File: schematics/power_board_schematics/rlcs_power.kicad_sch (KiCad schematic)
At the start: 44 parts, among them J1 Conn_01x05_Male, J2 Conn_01x05_Male, J3 Screw_Terminal_01x02, J4 Screw_Terminal_01x02, J5 Battery Conn, J6 Screw_Terminal_01x02, J7 Screw_Terminal_01x02, J8 CONN_01X02, Q1 Q_NPN_BEC, Q2 Q_NPN_BEC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

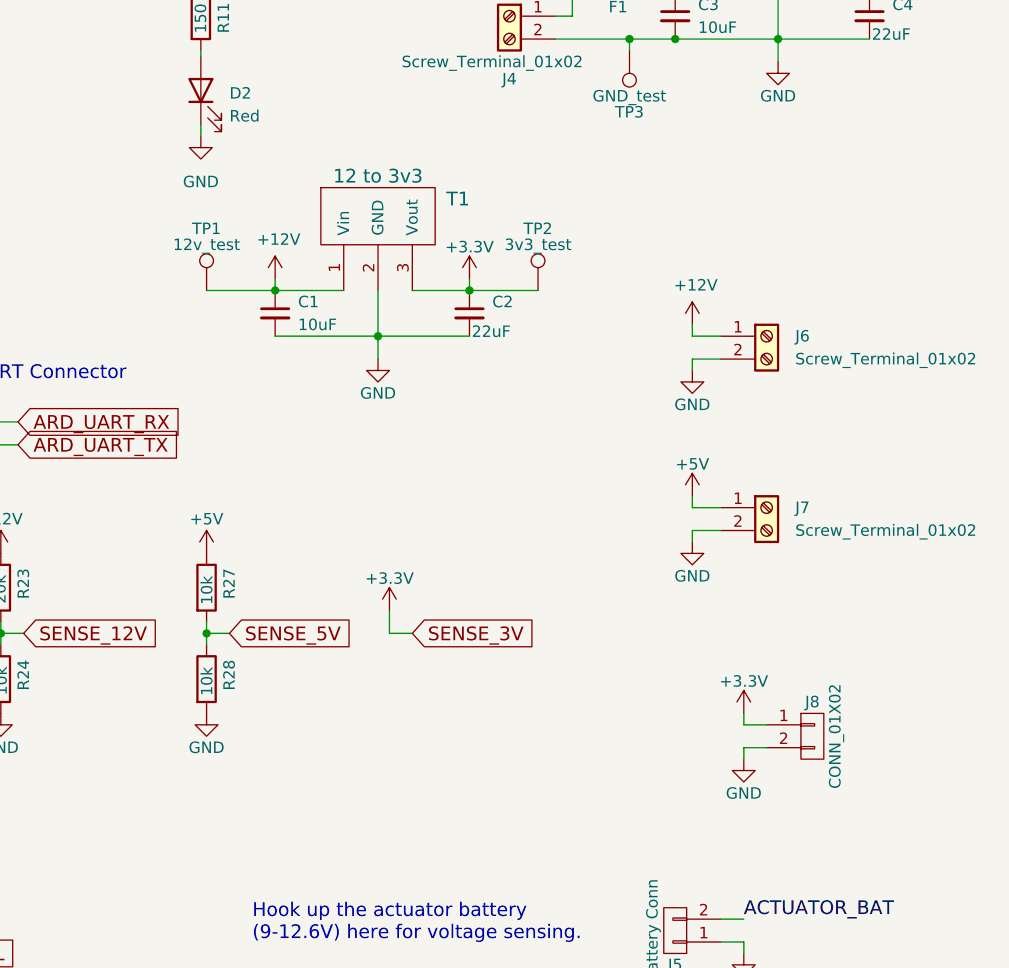
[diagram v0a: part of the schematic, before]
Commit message: Remove 3.3V circuit from Towerside Power Board
Remove 3.3V regulator
Remove 3.3V sensing
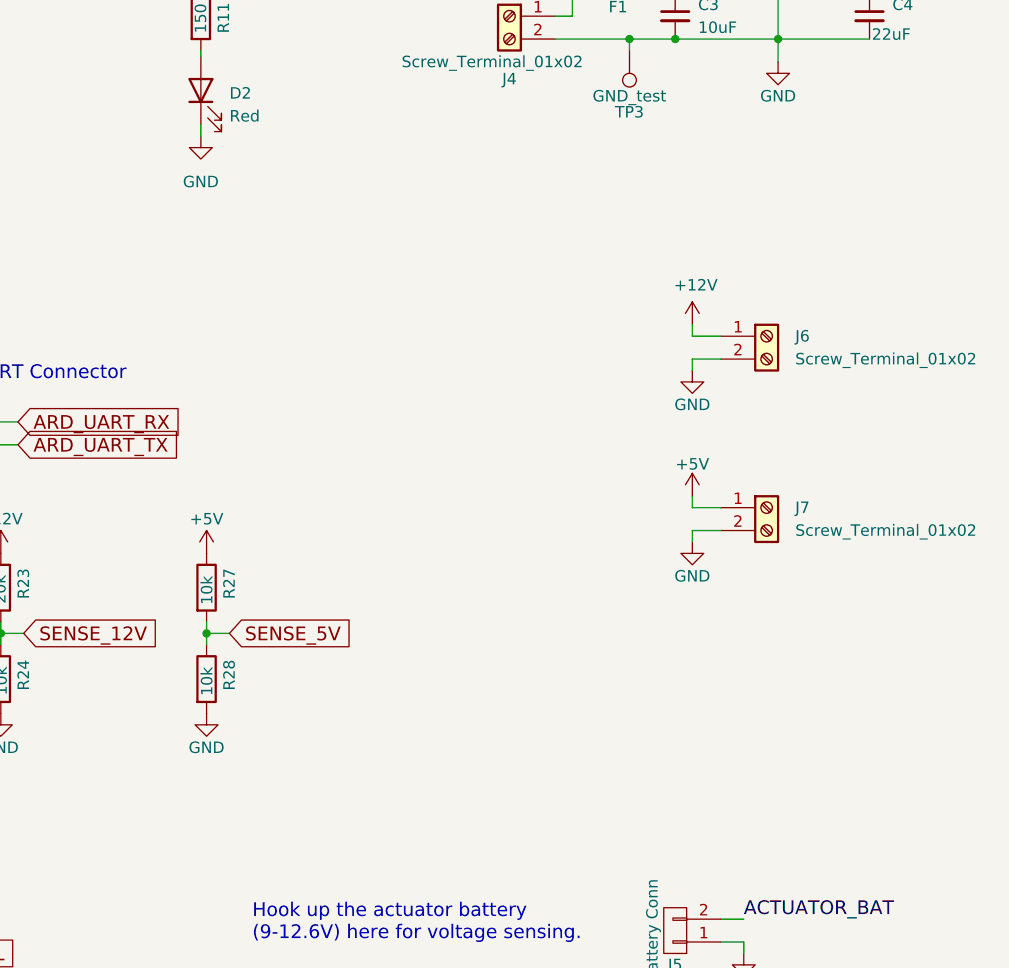
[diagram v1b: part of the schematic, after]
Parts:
- removed C1: 10uF, Capacitor_SMD:C_0805_2012Metric_Pad1.15x1.40mm_HandSolder, symbol Device:C_Small
- removed C2: 22uF, Capacitor_SMD:C_0805_2012Metric_Pad1.15x1.40mm_HandSolder, symbol Device:C_Small
- removed J8: CONN_01X02, Connector_Molex:Molex_KK-254_AE-6410-02A_1x02_P2.54mm_Vertical, symbol rlcs_power-rescue:CONN_01X02
- removed T1: 12 to 3v3, rlcs_power_footprints:VXO78XX-1000, symbol custom:MEZD71201A-G
- removed TP1: 12v_test, Connector_PinSocket_2.00mm:PinSocket_1x01_P2.00mm_Vertical, symbol rlcs_power-rescue:TEST_1P
- removed TP2: 3v3_test, Connector_PinSocket_2.00mm:PinSocket_1x01_P2.00mm_Vertical, symbol rlcs_power-rescue:TEST_1P

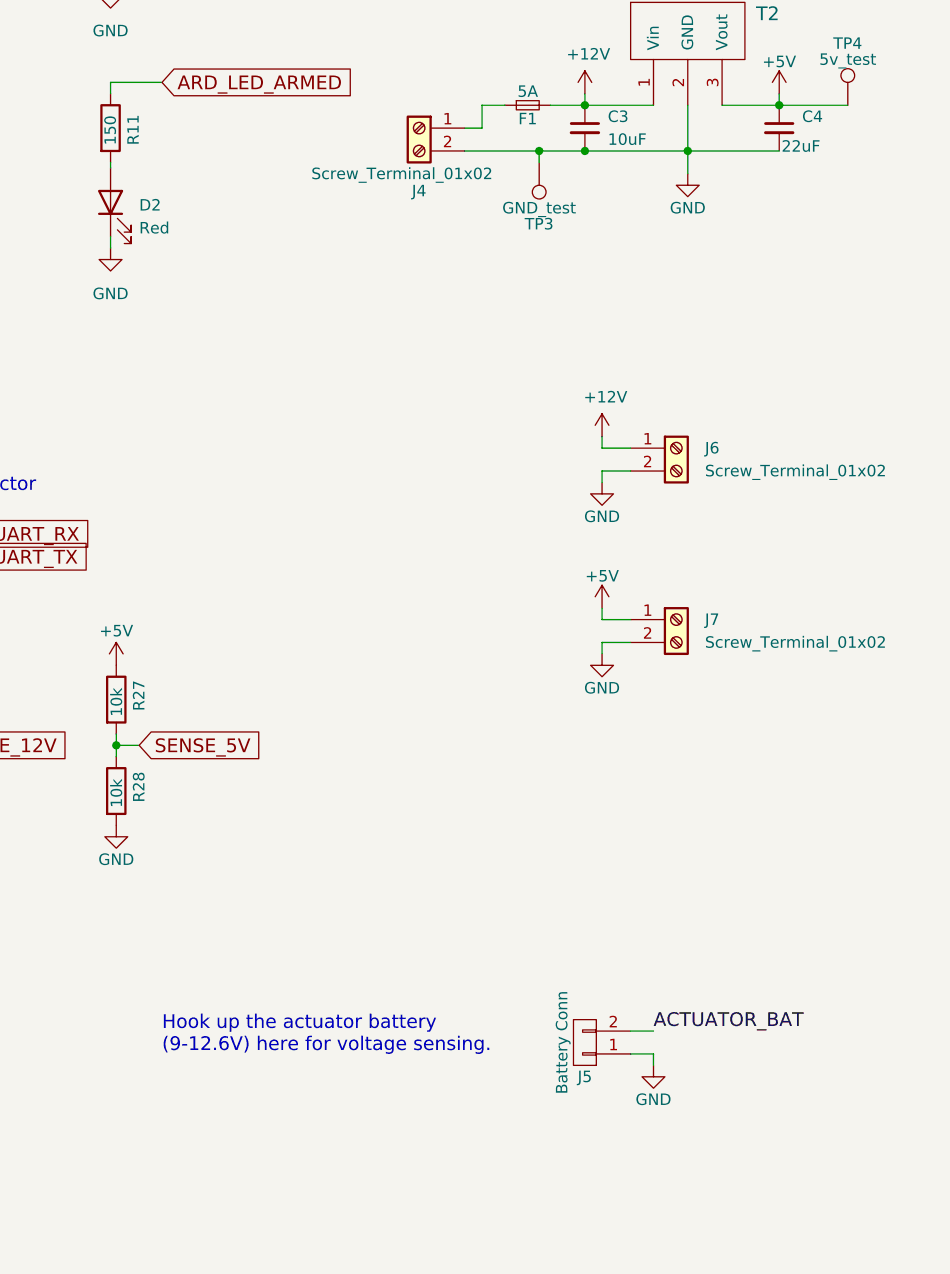
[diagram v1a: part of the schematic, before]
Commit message: Replace actuator battery connector with a screw terminal on Towerside Power Board
Replace J4 battery connection with a larger screw terminal
Use large screw terminal for J5 actuator battery connection
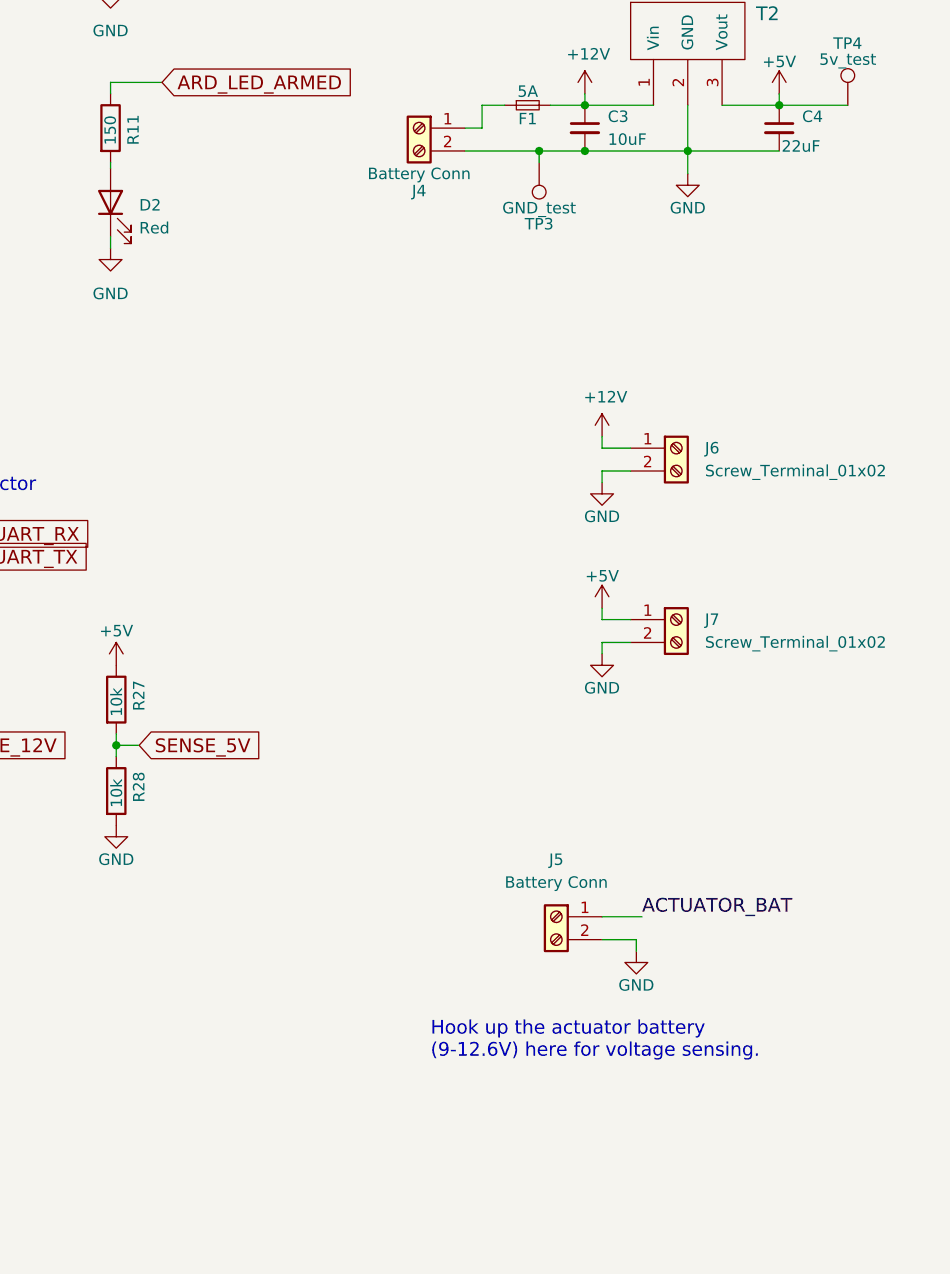
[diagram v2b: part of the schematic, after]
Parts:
- removed J5: Battery Conn, TerminalBlock_Phoenix:TerminalBlock_Phoenix_MKDS-1,5-2_1x02_P5.00mm_Horizontal, symbol rlcs_power-rescue:CONN_01X02
- added J5: Battery Conn, TerminalBlock_Phoenix:TerminalBlock_Phoenix_MKDS-1,5-2-5.08_1x02_P5.08mm_Horizontal, symbol Connector:Screw_Terminal_01x02
- J4: value Screw_Terminal_01x02 -> Battery Conn; footprint TerminalBlock_Phoenix:TerminalBlock_Phoenix_PT-1,5-2-5.0-H_1x02_P5.00mm_Horizontal -> TerminalBlock_Phoenix:TerminalBlock_Phoenix_MKDS-1,5-2-5.08_1x02_P5.08mm_Horizontal
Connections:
- net ACTUATOR_BAT: now also J5.1 (Pin_1)
- net GND: now also J5.2 (Pin_2)
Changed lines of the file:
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@@
+    (stroke (width 0) (type default) (color 0 0 0 0))
+  )
+  (wire (pts (xy 245.745 139.7) (xy 249.555 139.7))
     (stroke (width 0) (type default) (color 0 0 0 0))
   )
@@
     (stroke (width 0) (type default) (color 0 0 0 0))
   )
-  (wire (pts (xy 251.46 152.4) (xy 251.46 153.67))
+  (wire (pts (xy 249.555 139.7) (xy 249.555 140.97))
     (stroke (width 0) (type default) (color 0 0 0 0))
   )
@@
     (stroke (width 0) (type default) (color 0 0 0 0))
   )
-  (wire (pts (xy 251.46 149.86) (xy 248.92 149.86))
-    (stroke (width 0) (type default) (color 0 0 0 0))
-  )
   (wire (pts (xy 43.18 133.35) (xy 38.1 133.35))
     (stroke (width 0) (type default) (color 0 0 0 0))
@@
     (stroke (width 0) (type default) (color 0 0 0 0))
   )
-  (wire (pts (xy 248.92 152.4) (xy 251.46 152.4))
-    (stroke (width 0) (type default) (color 0 0 0 0))
-  )
   (wire (pts (xy 191.77 118.11) (xy 191.77 116.84))
     (stroke (width 0) (type default) (color 0 0 0 0))
@@
     (stroke (width 0) (type default) (color 0 0 0 0))
   )
+  (wire (pts (xy 245.745 137.16) (xy 250.19 137.16))
+    (stroke (width 0) (type default) (color 0 0 0 0))
+  )
   (wire (pts (xy 132.08 163.83) (xy 132.08 148.59))
     (stroke (width 0) (type default) (color 0 0 0 0))
@@
   )
   (text "Hook up the actuator battery\n(9-12.6V) here for voltage sensing."
-    (at 196.85 152.4 0)
+    (at 226.695 153.035 0)
     (effects (font (size 1.524 1.524)) (justify left bottom))
   )
@@
     (effects (font (size 1.524 1.524)) (justify left bottom))
   )
-  (label "ACTUATOR_BAT" (at 251.46 149.86 0)
+  (label "ACTUATOR_BAT" (at 250.19 137.16 0)
     (effects (font (size 1.524 1.524)) (justify left bottom))
   )
@@
     (in_bom yes) (on_board yes)
     (property "Reference" "J4" (id 0) (at 225.425 56.515 0))
-    (property "Value" "Screw_Terminal_01x02" (id 1) (at 223.52 54.61 0))
-    (property "Footprint" "TerminalBlock_Phoenix:TerminalBlock_Phoenix_PT-1,5-2-5.0-H_1x02_P5.00mm_Horizontal" (id 2) (at 225.425 49.53 0)
+    (property "Value" "Battery Conn" (id 1) (at 225.425 54.61 0))
+    (property "Footprint" "TerminalBlock_Phoenix:TerminalBlock_Phoenix_MKDS-1,5-2-5.08_1x02_P5.08mm_Horizontal" (id 2) (at 225.425 49.53 0)
       (effects (font (size 1.27 1.27)) hide)
     )
@@
     (pin "2")
   )
-  (symbol (lib_id "rlcs_power-rescue:CONN_01X02") (at 243.84 151.13 180) (unit 1)
-    (in_bom yes) (on_board yes)
-    (property "Reference" "J5" (id 0) (at 243.84 154.94 0))
-    (property "Value" "Battery Conn" (id 1) (at 241.3 151.13 90))
-    (property "Footprint" "TerminalBlock_Phoenix:TerminalBlock_Phoenix_MKDS-1,5-2_1x02_P5.00mm_Horizontal" (id 2) (at 243.84 151.13 0)
-      (effects (font (size 1.27 1.27)) hide)
-    )
-    (property "Datasheet" "" (id 3) (at 243.84 151.13 0)
+  (symbol (lib_id "Connector:Screw_Terminal_01x02") (at 240.665 137.16 0) (mirror y) (unit 1)
+    (in_bom yes) (on_board yes) (fields_autoplaced)
+    (property "Reference" "J5" (id 0) (at 240.665 130.81 0))
+    (property "Value" "Battery Conn" (id 1) (at 240.665 133.35 0))
+    (property "Footprint" "TerminalBlock_Phoenix:TerminalBlock_Phoenix_MKDS-1,5-2-5.08_1x02_P5.08mm_Horizontal" (id 2) (at 240.665 137.16 0)
+      (effects (font (size 1.27 1.27)) hide)
+    )
+    (property "Datasheet" "~" (id 3) (at 240.665 137.16 0)
       (effects (font (size 1.27 1.27)) hide)
     )
@@
     (pin "2")
   )
-  (symbol (lib_id "power:GND") (at 251.46 153.67 0) (mirror y) (unit 1)
-    (in_bom yes) (on_board yes)
-    (property "Reference" "#PWR032" (id 0) (at 251.46 160.02 0)
-      (effects (font (size 1.27 1.27)) hide)
-    )
-    (property "Value" "GND" (id 1) (at 251.46 157.48 0))
-    (property "Footprint" "" (id 2) (at 251.46 153.67 0)
-      (effects (font (size 1.27 1.27)) hide)
-    )
-    (property "Datasheet" "" (id 3) (at 251.46 153.67 0)
+  (symbol (lib_id "power:GND") (at 249.555 140.97 0) (mirror y) (unit 1)
+    (in_bom yes) (on_board yes)
+    (property "Reference" "#PWR032" (id 0) (at 249.555 147.32 0)
+      (effects (font (size 1.27 1.27)) hide)
+    )
+    (property "Value" "GND" (id 1) (at 249.555 144.78 0))
+    (property "Footprint" "" (id 2) (at 249.555 140.97 0)
+      (effects (font (size 1.27 1.27)) hide)
+    )
+    (property "Datasheet" "" (id 3) (at 249.555 140.97 0)
       (effects (font (size 1.27 1.27)) hide)
     )
@@
     )
     (path "/b64e4836-489c-446c-918c-b81c58ceb09e"
-      (reference "J4") (unit 1) (value "Screw_Terminal_01x02") (footprint "TerminalBlock_Phoenix:TerminalBlock_Phoenix_PT-1,5-2-5.0-H_1x02_P5.00mm_Horizontal")
-    )
-    (path "/c0b62577-bcd8-4917-8a4c-0ff5043047f2"
-      (reference "J5") (unit 1) (value "Battery Conn") (footprint "TerminalBlock_Phoenix:TerminalBlock_Phoenix_MKDS-1,5-2_1x02_P5.00mm_Horizontal")
+      (reference "J4") (unit 1) (value "Battery Conn") (footprint "TerminalBlock_Phoenix:TerminalBlock_Phoenix_MKDS-1,5-2-5.08_1x02_P5.08mm_Horizontal")
+    )
+    (path "/b66cf642-a1dc-4e74-85e6-669f964b45aa"
+      (reference "J5") (unit 1) (value "Battery Conn") (footprint "TerminalBlock_Phoenix:TerminalBlock_Phoenix_MKDS-1,5-2-5.08_1x02_P5.08mm_Horizontal")
     )
     (path "/3ff96f21-873b-473c-a7ea-332f0c31db33"

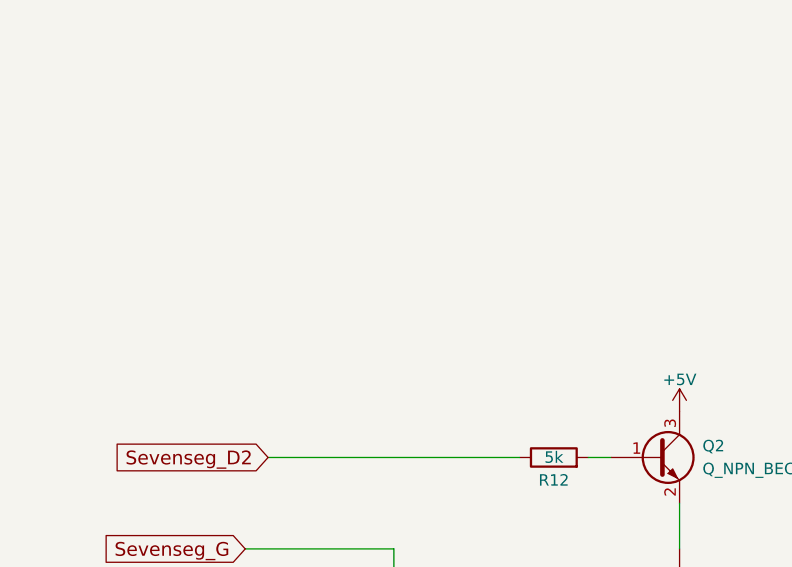
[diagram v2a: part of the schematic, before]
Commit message: Add arming switch connector to Towerside Power Board
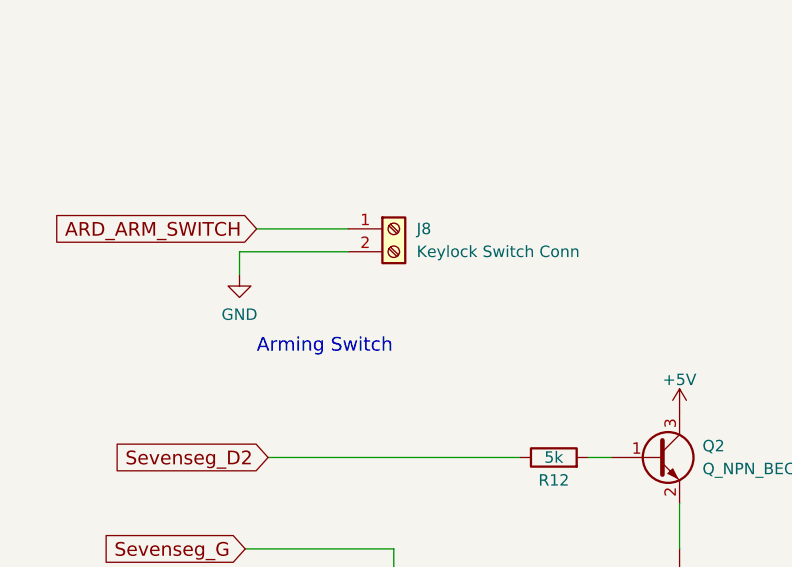
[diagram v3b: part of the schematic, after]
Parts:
- added J8: Keylock Switch Conn, symbol Connector:Screw_Terminal_01x02
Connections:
- net GND: now also J8.2 (Pin_2)
- new net ARD_ARM_SWITCH: J8.1 (Pin_1)
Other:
- note added: "Arming Switch"
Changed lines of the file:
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@@
+    (stroke (width 0) (type default) (color 0 0 0 0))
+  )
+  (wire (pts (xy 39.37 77.47) (xy 49.53 77.47))
     (stroke (width 0) (type default) (color 0 0 0 0))
   )
@@
     (stroke (width 0) (type default) (color 0 0 0 0))
   )
+  (wire (pts (xy 37.465 80.01) (xy 49.53 80.01))
+    (stroke (width 0) (type default) (color 0 0 0 0))
+  )
   (wire (pts (xy 113.03 158.75) (xy 139.7 158.75))
     (stroke (width 0) (type default) (color 0 0 0 0))
@@
   )
   (wire (pts (xy 86.36 107.95) (xy 86.36 113.03))
+    (stroke (width 0) (type default) (color 0 0 0 0))
+  )
+  (wire (pts (xy 37.465 82.55) (xy 37.465 80.01))
     (stroke (width 0) (type default) (color 0 0 0 0))
   )
@@
   )
   (text "Power section\n- let other ICs do it\n" (at 222.885 30.48 0)
+    (effects (font (size 1.524 1.524)) (justify left bottom))
+  )
+  (text "Arming Switch" (at 39.37 91.44 0)
     (effects (font (size 1.524 1.524)) (justify left bottom))
   )
@@
     (property "Intersheet References" "${INTERSHEET_REFS}" (id 0) (at 217.9269 44.3548 0)
       (effects (font (size 1.524 1.524)) (justify left) hide)
+    )
+  )
+  (global_label "ARD_ARM_SWITCH" (shape input) (at 39.37 77.47 180) (fields_autoplaced)
+    (effects (font (size 1.524 1.524)) (justify right))
+    (property "Intersheet References" "${INTERSHEET_REFS}" (id 0) (at 17.132 77.3748 0)
+      (effects (font (size 1.524 1.524)) (justify right) hide)
     )
   )
@@
     (pin "2")
   )
+  (symbol (lib_id "Connector:Screw_Terminal_01x02") (at 54.61 77.47 0) (unit 1)
+    (in_bom yes) (on_board yes) (fields_autoplaced)
+    (property "Reference" "J8" (id 0) (at 57.15 77.4699 0)
+      (effects (font (size 1.27 1.27)) (justify left))
+    )
+    (property "Value" "Keylock Switch Conn" (id 1) (at 57.15 80.0099 0)
+      (effects (font (size 1.27 1.27)) (justify left))
+    )
+    (property "Footprint" "" (id 2) (at 54.61 77.47 0)
+      (effects (font (size 1.27 1.27)) hide)
+    )
+    (property "Datasheet" "~" (id 3) (at 54.61 77.47 0)
+      (effects (font (size 1.27 1.27)) hide)
+    )
+    (pin "1")
+    (pin "2")
+  )
   (symbol (lib_id "power:+5V") (at 191.77 109.22 0) (unit 1)
     (in_bom yes) (on_board yes)
@@
     (pin "1")
     (pin "2")
+  )
+  (symbol (lib_id "power:GND") (at 37.465 82.55 0) (unit 1)
+    (in_bom yes) (on_board yes) (fields_autoplaced)
+    (property "Reference" "#PWR0103" (id 0) (at 37.465 88.9 0)
+      (effects (font (size 1.27 1.27)) hide)
+    )
+    (property "Value" "GND" (id 1) (at 37.465 86.995 0))
+    (property "Footprint" "" (id 2) (at 37.465 82.55 0)
+      (effects (font (size 1.27 1.27)) hide)
+    )
+    (property "Datasheet" "" (id 3) (at 37.465 82.55 0)
+      (effects (font (size 1.27 1.27)) hide)
+    )
+    (pin "1")
   )
   (symbol (lib_id "power:+12V") (at 168.91 109.22 0) (unit 1)
@@
       (reference "#PWR0102") (unit 1) (value "GND") (footprint "")
     )
+    (path "/4bfab255-ee88-4eab-b699-95f5ad07b9fb"
+      (reference "#PWR0103") (unit 1) (value "GND") (footprint "")
+    )
     (path "/00000000-0000-0000-0000-000059c5bada"
       (reference "AFF1") (unit 1) (value "LTD-4608JR") (footprint "rlcs_power:LTD-4608JR")
@@
       (reference "J7") (unit 1) (value "Screw_Terminal_01x02") (footprint "TerminalBlock_Phoenix:TerminalBlock_Phoenix_PT-1,5-2-5.0-H_1x02_P5.00mm_Horizontal")
     )
+    (path "/0a81f968-d32d-4e4d-acbd-0519aedcf51c"
+      (reference "J8") (unit 1) (value "Keylock Switch Conn") (footprint "")
+    )
     (path "/00000000-0000-0000-0000-000059ca1e66"
